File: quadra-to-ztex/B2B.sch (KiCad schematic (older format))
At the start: 8 parts, among them J1 Conn_02x07_Odd_Even

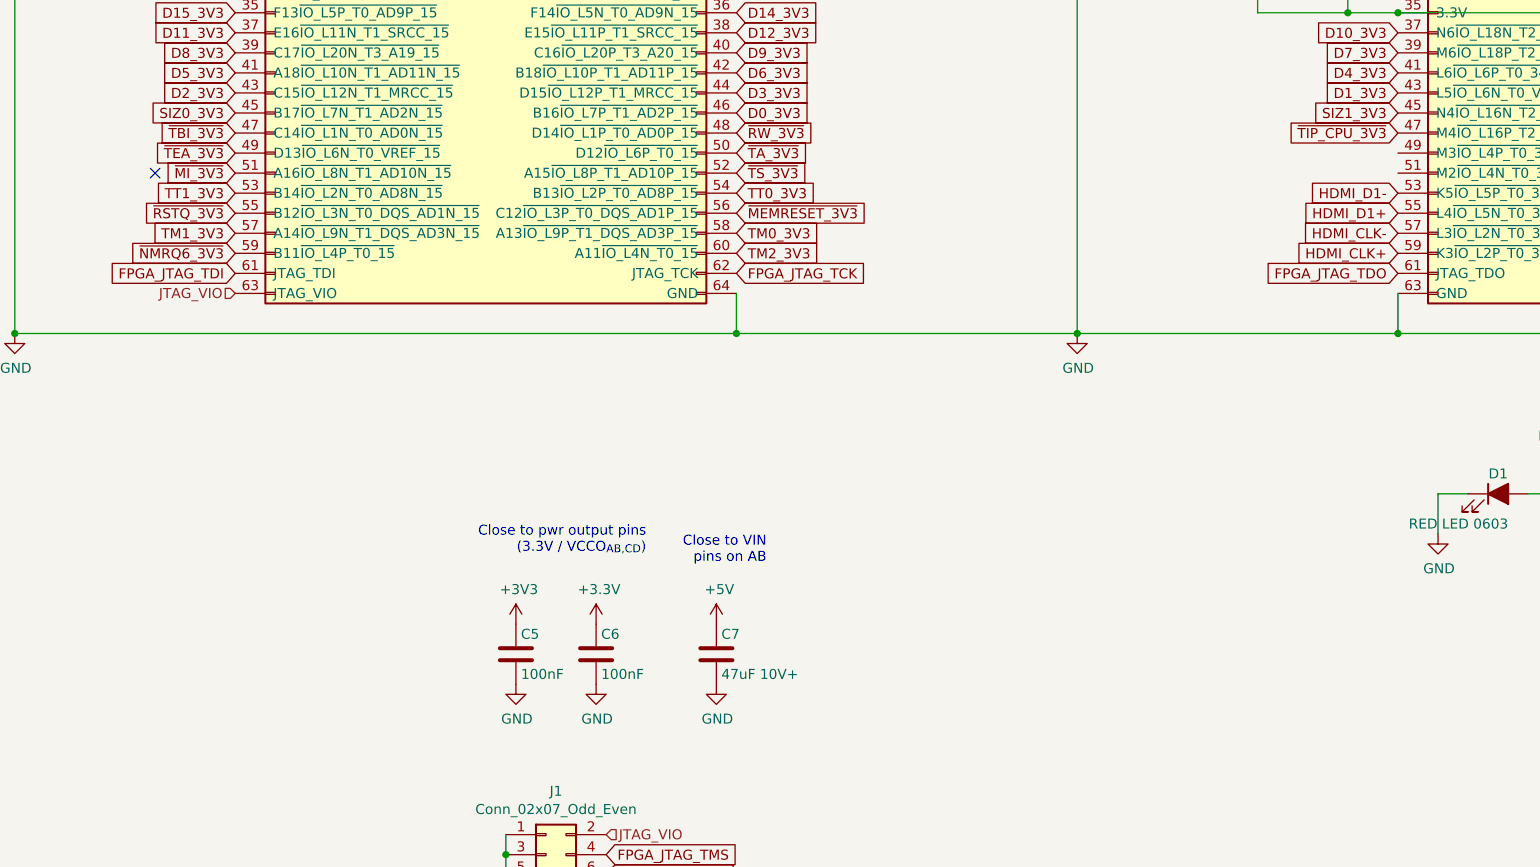
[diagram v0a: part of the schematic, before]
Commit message: remove memreset, add busmastering (?)
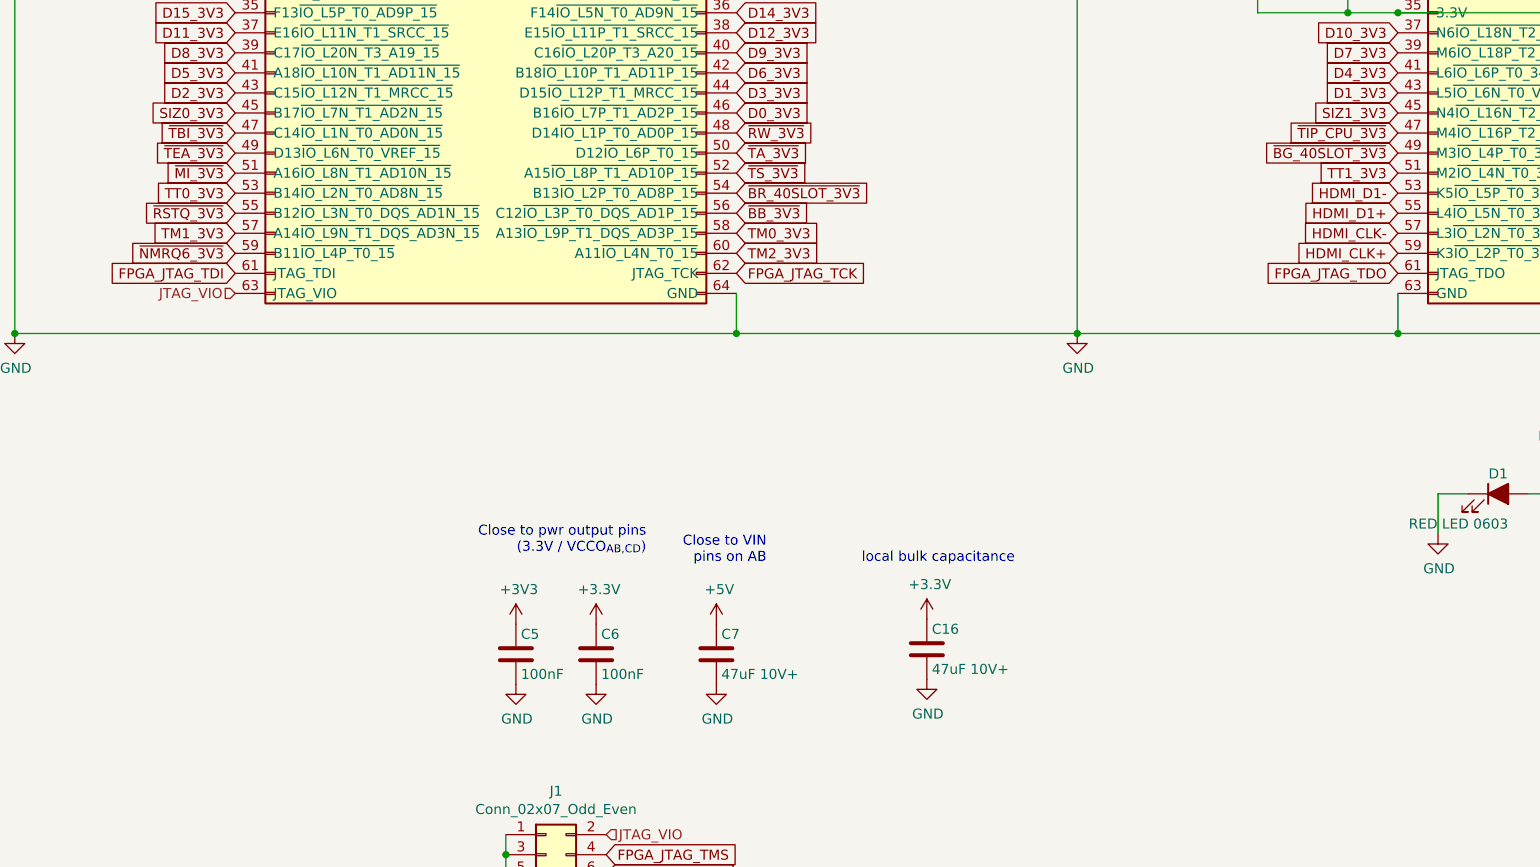
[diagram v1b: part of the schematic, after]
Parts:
- added C16: 47uF 10V+, Capacitor_SMD:C_1206_3216Metric, symbol Device:C
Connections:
- net +3V3: now also C16.1
- net GND: now also C16.2
- net TT0_3V3: now also JAB1.53 (B14~IO_L2N_T0_AD8N_15); no longer JAB1.54 (B13~IO_L2P_T0_AD8P_15)
- net TT1_3V3: now also JCD1.51 (M2~IO_L4N_T0_34); no longer JAB1.53 (B14~IO_L2N_T0_AD8N_15)
- net ~BG_40SLOT_3V3: now reaches JCD1.49 (M3~IO_L4P_T0_34)
- net ~MEMRESET_3V3 renamed ~BB_3V3
- new net ~BR_40SLOT_3V3: JAB1.54 (B13~IO_L2P_T0_AD8P_15)
- no-connect marks 3 -> 2
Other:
- note added: "local bulk capacitance"
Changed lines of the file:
@@
 Text GLabel 1600 3650 0    50   Input ~ 0
 ~MI_3V3
-Text GLabel 4100 3750 2    50   Input ~ 0
+Text GLabel 1600 3750 0    50   Input ~ 0
 TT0_3V3
-Text GLabel 1600 3750 0    50   Input ~ 0
+Text GLabel 7400 3650 0    50   Input ~ 0
 TT1_3V3
-Text GLabel 4100 3850 2    50   Input ~ 0
-~MEMRESET_3V3
 Text GLabel 1600 3850 0    50   Input ~ 0
 ~RSTQ_3V3
@@
 Text GLabel 9900 3150 2    50   Input ~ 0
 PMOD-910+
-NoConn ~ 1200 3650
+Text GLabel 7400 3550 0    50   Input ~ 0
+~BG_40SLOT_3V3
+Text GLabel 4100 3750 2    50   Input ~ 0
+~BR_40SLOT_3V3
+Text GLabel 4100 3850 2    50   Input ~ 0
+~BB_3V3
+$Comp
+L Device:C C?
+U 1 1 6507C211
+P 5050 6025
+AR Path="/5F69F4EF/6507C211" Ref="C?"  Part="1"
+AR Path="/5F6B165A/6507C211" Ref="C?"  Part="1"
+AR Path="/61B99D2C/6507C211" Ref="C?"  Part="1"
+AR Path="/618E8C75/6507C211" Ref="C?"  Part="1"
+AR Path="/631F3844/6507C211" Ref="C?"  Part="1"
+AR Path="/6432B233/6507C211" Ref="C?"  Part="1"
+AR Path="/65D4166B/6507C211" Ref="C16"  Part="1"
+F 0 "C16" H 5075 6125 50  0000 L CNN
+F 1 "47uF 10V+" H 5075 5925 50  0000 L CNN
+F 2 "Capacitor_SMD:C_1206_3216Metric" H 5088 5875 50  0001 C CNN
+F 3 "" H 5050 6025 50  0000 C CNN
+F 4 "CL31A476MPHNNNE" H 5050 6025 50  0001 C CNN "MPN"
+F 5 "https://www.lcsc.com/product-detail/Multilayer-Ceramic-Capacitors-MLCC-SMD-SMT_Samsung-Electro-Mechanics-CL31A476MPHNNNE_C96123.html" H 5050 6025 50  0001 C CNN "URL"
+	1    5050 6025
+	1    0    0    -1
+$EndComp
+$Comp
+L power:GND #PWR0158
+U 1 1 6507C217
+P 5050 6175
+F 0 "#PWR0158" H 5050 5925 50  0001 C CNN
+F 1 "GND" H 5055 6002 50  0000 C CNN
+F 2 "" H 5050 6175 50  0001 C CNN
+F 3 "" H 5050 6175 50  0001 C CNN
+	1    5050 6175
+	1    0    0    -1
+$EndComp
+$Comp
+L power:+3.3V #PWR0159
+U 1 1 6507D249
+P 5050 5875
+F 0 "#PWR0159" H 5050 5725 50  0001 C CNN
+F 1 "+3.3V" H 5065 6048 50  0000 C CNN
+F 2 "" H 5050 5875 50  0001 C CNN
+F 3 "" H 5050 5875 50  0001 C CNN
+	1    5050 5875
+	1    0    0    -1
+$EndComp
+Text Notes 4725 5600 0    50   ~ 0
+local bulk capacitance
 $EndSCHEMATC

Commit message: upd gen files
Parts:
- JAB1, JCD1: MPN-ALT (none) -> X6521WV-2x32H-C30D60
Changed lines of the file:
@@
 F 3 "" H 7600 2650 50  0001 C CNN
 F 4 "77313-824-64LF" H 7600 2650 50  0001 C CNN "MPN"
+F 5 "X6521WV-2x32H-C30D60" H 7600 2650 50  0001 C CNN "MPN-ALT"
 	1    7600 2650
 	1    0    0    -1
@@
 F 3 "" H 1800 2650 50  0001 C CNN
 F 4 "77313-824-64LF" H 1800 2650 50  0001 C CNN "MPN"
+F 5 "X6521WV-2x32H-C30D60" H 1800 2650 50  0001 C CNN "MPN-ALT"
 	1    1800 2650
 	1    0    0    -1

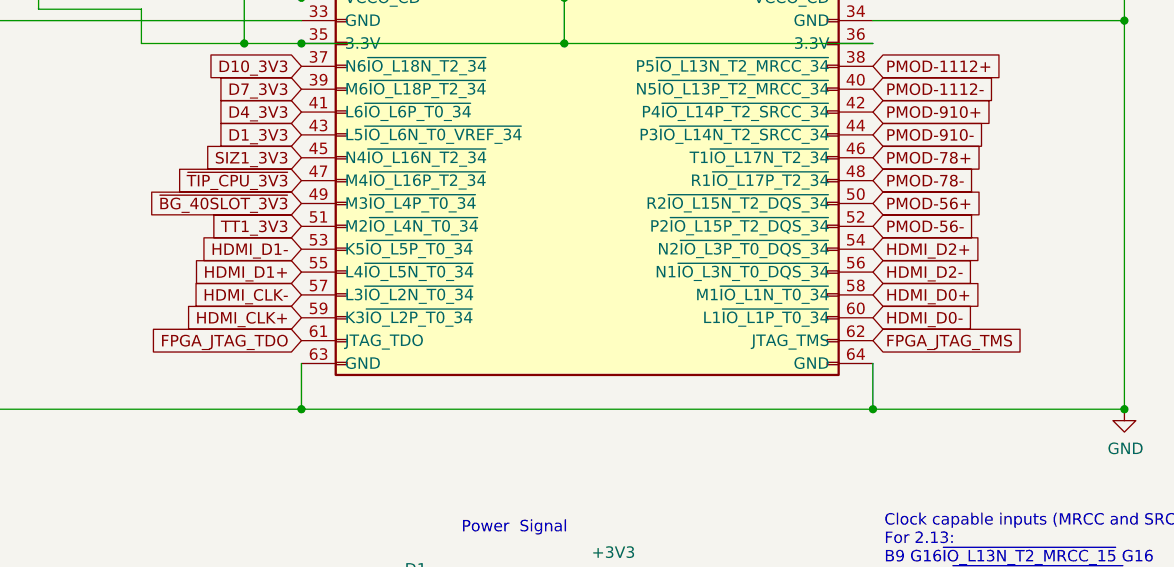
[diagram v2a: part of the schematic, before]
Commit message: rewire to avoid p/n conflicts
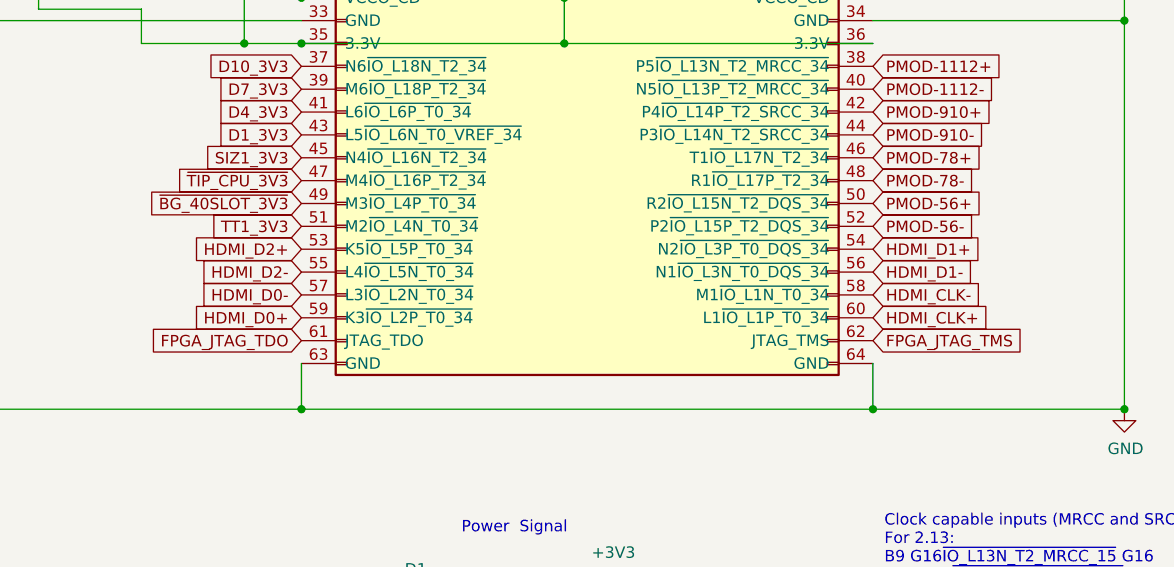
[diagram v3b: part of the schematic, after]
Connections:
- net HDMI_CLK+: now also JCD1.60 (L1~IO_L1P_T0_34); no longer JCD1.59 (K3~IO_L2P_T0_34)
- net HDMI_CLK-: now also JCD1.58 (M1~IO_L1N_T0_34); no longer JCD1.57 (L3~IO_L2N_T0_34)
- net HDMI_D0+: now also JCD1.59 (K3~IO_L2P_T0_34); no longer JCD1.58 (M1~IO_L1N_T0_34)
- net HDMI_D0-: now also JCD1.57 (L3~IO_L2N_T0_34); no longer JCD1.60 (L1~IO_L1P_T0_34)
- net HDMI_D1+: now also JCD1.54 (N2~IO_L3P_T0_DQS_34); no longer JCD1.55 (L4~IO_L5N_T0_34)
- net HDMI_D1-: now also JCD1.56 (N1~IO_L3N_T0_DQS_34); no longer JCD1.53 (K5~IO_L5P_T0_34)
- net HDMI_D2+: now also JCD1.53 (K5~IO_L5P_T0_34); no longer JCD1.54 (N2~IO_L3P_T0_DQS_34)
- net HDMI_D2-: now also JCD1.55 (L4~IO_L5N_T0_34); no longer JCD1.56 (N1~IO_L3N_T0_DQS_34)
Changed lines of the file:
@@
 Text GLabel 9900 1750 2    50   Input ~ 0
 A10_3V3
+Text GLabel 9900 4050 2    50   Input ~ 0
+HDMI_CLK+
+Text GLabel 9900 3950 2    50   Input ~ 0
+HDMI_CLK-
 Text GLabel 7400 4050 0    50   Input ~ 0
-HDMI_CLK+
+HDMI_D0+
 Text GLabel 7400 3950 0    50   Input ~ 0
-HDMI_CLK-
-Text GLabel 9900 3950 2    50   Input ~ 0
-HDMI_D0+
-Text GLabel 9900 4050 2    50   Input ~ 0
 HDMI_D0-
+Text GLabel 9900 3750 2    50   Input ~ 0
+HDMI_D1+
+Text GLabel 9900 3850 2    50   Input ~ 0
+HDMI_D1-
+Text GLabel 7400 3750 0    50   Input ~ 0
+HDMI_D2+
 Text GLabel 7400 3850 0    50   Input ~ 0
-HDMI_D1+
-Text GLabel 7400 3750 0    50   Input ~ 0
-HDMI_D1-
-Text GLabel 9900 3750 2    50   Input ~ 0
-HDMI_D2+
-Text GLabel 9900 3850 2    50   Input ~ 0
 HDMI_D2-
 Text GLabel 7400 2050 0    50   Input ~ 0

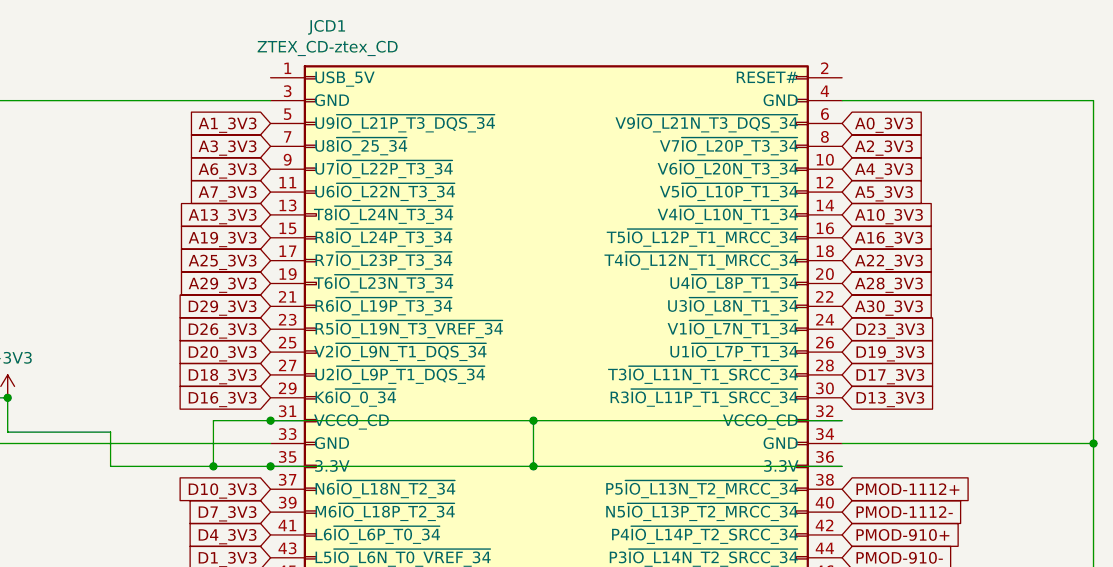
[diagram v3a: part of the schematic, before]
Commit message: fix A18 <-> A19 (hardware)
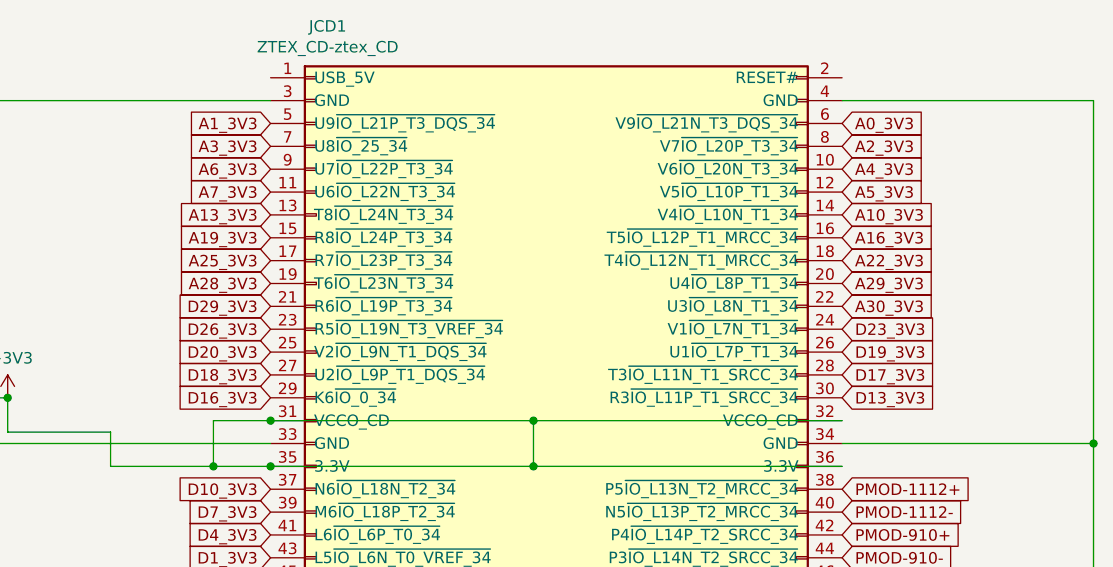
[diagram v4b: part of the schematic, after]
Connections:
- net A28_3V3: now also JCD1.19 (T6~IO_L23N_T3_34); no longer JCD1.20 (U4~IO_L8P_T1_34)
- net A29_3V3: now also JCD1.20 (U4~IO_L8P_T1_34); no longer JCD1.19 (T6~IO_L23N_T3_34)
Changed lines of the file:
@@
 Text GLabel 1600 1550 0    50   Input ~ 0
 A15_3V3
-Text GLabel 9900 2050 2    50   Input ~ 0
+Text GLabel 7400 2050 0    50   Input ~ 0
 A28_3V3
 Text GLabel 1600 1950 0    50   Input ~ 0
@@
 Text GLabel 7400 3850 0    50   Input ~ 0
 HDMI_D2-
-Text GLabel 7400 2050 0    50   Input ~ 0
+Text GLabel 9900 2050 2    50   Input ~ 0
 A29_3V3
 Text GLabel 9900 2150 2    50   Input ~ 0
